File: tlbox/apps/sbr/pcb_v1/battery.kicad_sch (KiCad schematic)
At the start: 1 part, among them J2 Conn_01x02_Pin

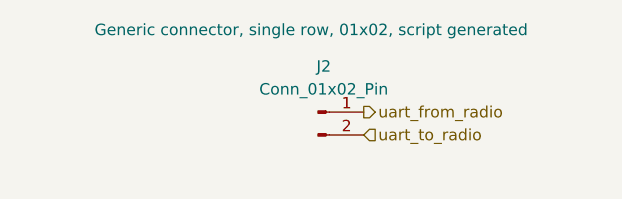
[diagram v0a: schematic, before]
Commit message: New schematic
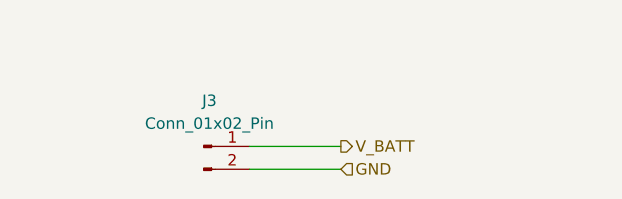
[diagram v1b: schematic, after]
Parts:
- removed J2: Conn_01x02_Pin, symbol Connector:Conn_01x02_Pin
- added J3: Conn_01x02_Pin, symbol Connector:Conn_01x02_Pin
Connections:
- new net GND: J3.2 (Pin_2)
- new net V_BATT: J3.1 (Pin_1)
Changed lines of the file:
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@@
 	(generator_version "10.0")
 	(paper "A4")
-	(hierarchical_label "uart_from_radio"
+	(wire
+		(pts
+			(xy 102.87 68.58) (xy 113.03 68.58)
+		)
+		(stroke
+			(width 0)
+			(type default)
+		)
+	)
+	(wire
+		(pts
+			(xy 102.87 66.04) (xy 113.03 66.04)
+		)
+		(stroke
+			(width 0)
+			(type default)
+		)
+	)
+	(hierarchical_label "V_BATT"
 		(shape output)
-		(at 115.57 62.23 0)
+		(at 113.03 66.04 0)
 		(effects
 			(font
@@
 		)
 	)
-	(hierarchical_label "uart_to_radio"
+	(hierarchical_label "GND"
 		(shape input)
-		(at 115.57 64.77 0)
+		(at 113.03 68.58 0)
 		(effects
 			(font
@@
 	(symbol
 		(lib_id "Connector:Conn_01x02_Pin")
-		(at 110.49 62.23 0)
+		(at 97.79 66.04 0)
 		(unit 1)
 		(body_style 1)
@@
 		(in_pos_files yes)
 		(dnp no)
-		(property "Reference" "J2"
-			(at 111.125 57.15 0)
+		(fields_autoplaced yes)
+		(property "Reference" "J3"
+			(at 98.425 60.96 0)
 			(show_name no)
 			(do_not_autoplace no)
@@
 		)
 		(property "Value" "Conn_01x02_Pin"
-			(at 111.125 59.69 0)
+			(at 98.425 63.5 0)
 			(show_name no)
 			(do_not_autoplace no)
@@
 		)
 		(property "Footprint" ""
-			(at 110.49 62.23 0)
+			(at 97.79 66.04 0)
 			(hide yes)
 			(show_name no)
@@
 		)
 		(property "Datasheet" ""
-			(at 110.49 62.23 0)
+			(at 97.79 66.04 0)
 			(hide yes)
 			(show_name no)
@@
 		)
 		(property "Description" "Generic connector, single row, 01x02, script generated"
-			(at 109.728 53.086 0)
+			(at 97.79 66.04 0)
+			(hide yes)
 			(show_name no)
 			(do_not_autoplace no)
@@
 			)
 		)
+		(pin "1"
+		)
 		(pin "2"
-		)
-		(pin "1"
 		)
 		(instances
 			(project "self_balancing_robot_v1"
-				(path "/f1bc52c2-82b2-44ac-a8ec-1286ff19a550/7849255e-dc2a-45a5-ad4e-6c6d20980213"
-					(reference "J2")
+				(path "/f1bc52c2-82b2-44ac-a8ec-1286ff19a550/94992c47-cb2c-4482-85ea-a7222cb63fbb"
+					(reference "J3")
 					(unit 1)
 				)
